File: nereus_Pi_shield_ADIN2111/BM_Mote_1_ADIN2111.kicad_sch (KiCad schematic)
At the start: 26 parts, among them U1 ADIN2111BCPZ, U2 AP22913CN4-7, U3 AP22913CN4-7, Y1 ABM11W-25.0000MHZ-6-K1Z-T3

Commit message: S4.d: footprints findable -- project library Vault (mote.pretty) extracted from the mote board; close S5.a
43 footprints the schematic uses, extracted read-only from the reference
board with KiCad 9.0.6 pcbnew (tools/fpextract.py, back-side parts
flipped, nets cleared), registered as nickname Vault to match the board
IDs; 118 bare footprint fields -> Vault:<name>. fpextract --verify: 0
problems (negative-tested). Netlist identical except footprint fields.
ERC 74/626 -> 74/508 (footprint-link warnings gone). D19.

Co-Authored-By: Claude Opus 5.5 <noreply@anthropic.com>
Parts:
- C1, C10, C11, C12, C13, C14, C3, C9: footprint FP-CL278-IPC_C -> Vault:FP-CL278-IPC_C
- C2, C4: footprint FP-CL511-IPC_C -> Vault:FP-CL511-IPC_C
- C5, C6: footprint FP-CC0402-MFG -> Vault:FP-CC0402-MFG
- C7, C8: footprint FP-CC0402-0_55-IPC_B -> Vault:FP-CC0402-0_55-IPC_B
- R1: footprint RESC1005X40X25ML05T10 -> Vault:RESC1005X40X25ML05T10
- R2, R3, R4, R5, R6: footprint RESC1005X40X25LL05T05 -> Vault:RESC1005X40X25LL05T05
- TP1, TP2: footprint PCB_TP_1.5mm -> Vault:PCB_TP_1.5mm
- U1: footprint ADIN2111BCPZ-Footprint-1 -> Vault:ADIN2111BCPZ-Footprint-1
- U2, U3: footprint AP22913CN4-7-Footprint-1 -> Vault:AP22913CN4-7-Footprint-1
- Y1: footprint FP-ABM11W-MFG -> Vault:FP-ABM11W-MFG
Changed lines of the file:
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@@
 			)
 		)
-		(property "Footprint" "PCB_TP_1.5mm"
+		(property "Footprint" "Vault:PCB_TP_1.5mm"
 			(at 185.42 200.4822 0)
 			(effects
@@
 			)
 		)
-		(property "Footprint" "RESC1005X40X25ML05T10"
+		(property "Footprint" "Vault:RESC1005X40X25ML05T10"
 			(at 121.92 70.9422 0)
 			(effects
@@
 			)
 		)
-		(property "Footprint" ""
+				(property "Footprint" ""
 			(at 91.44 96.3422 0)
 			(effects
@@
 			)
 		)
-		(property "Footprint" ""
+				(property "Footprint" ""
 			(at 215.9 238.5822 0)
 			(effects
@@
 			)
 		)
-		(property "Footprint" ""
+				(property "Footprint" ""
 			(at 226.06 238.5822 0)
 			(effects
@@
 			)
 		)
-		(property "Footprint" "ADIN2111BCPZ-Footprint-1"
+		(property "Footprint" "Vault:ADIN2111BCPZ-Footprint-1"
 			(at 259.08 203.0222 0)
 			(effects
@@
 			)
 		)
-		(property "Footprint" "FP-CL278-IPC_C"
+		(property "Footprint" "Vault:FP-CL278-IPC_C"
 			(at 226.06 228.4222 0)
 			(effects
@@
 			)
 		)
-		(property "Footprint" "PCB_TP_1.5mm"
+		(property "Footprint" "Vault:PCB_TP_1.5mm"
 			(at 185.42 230.9622 0)
 			(effects
@@
 			)
 		)
-		(property "Footprint" ""
+				(property "Footprint" ""
 			(at 160.02 91.2622 0)
 			(effects
@@
 			)
 		)
-		(property "Footprint" "AP22913CN4-7-Footprint-1"
+		(property "Footprint" "Vault:AP22913CN4-7-Footprint-1"
 			(at 177.8 228.4222 0)
 			(effects
@@
 			)
 		)
-		(property "Footprint" ""
+				(property "Footprint" ""
 			(at 264.16 78.5622 0)
 			(effects
@@
 			)
 		)
-		(property "Footprint" ""
+				(property "Footprint" ""
 			(at 287.02 103.9622 0)
 			(effects
@@
 			)
 		)
-		(property "Footprint" "FP-CL278-IPC_C"
+		(property "Footprint" "Vault:FP-CL278-IPC_C"
 			(at 276.86 70.9422 0)
 			(effects
@@
 			)
 		)
-		(property "Footprint" "FP-CC0402-MFG"
+		(property "Footprint" "Vault:FP-CC0402-MFG"
 			(at 91.44 88.7222 0)
 			(effects
@@
 			)
 		)
-		(property "Footprint" ""
+				(property "Footprint" ""
 			(at 264.16 106.5022 0)
 			(effects
@@
 			)
 		)
-		(property "Footprint" "RESC1005X40X25LL05T05"
+		(property "Footprint" "Vault:RESC1005X40X25LL05T05"
 			(at 254 106.5022 0)
 			(effects
@@
 			)
 		)
-		(property "Footprint" ""
+				(property "Footprint" ""
 			(at 124.46 63.3222 0)
 			(effects
@@
 			)
 		)
-		(property "Footprint" ""
+				(property "Footprint" ""
 			(at 78.74 93.8022 0)
 			(effects
@@
 			)
 		)
-		(property "Footprint" ""
+				(property "Footprint" ""
 			(at 264.16 119.2022 0)
 			(effects
@@
 			)
 		)
-		(property "Footprint" "RESC1005X40X25LL05T05"
+		(property "Footprint" "Vault:RESC1005X40X25LL05T05"
 			(at 261.62 91.2622 0)
 			(effects
@@
 			)
 		)
-		(property "Footprint" ""
+				(property "Footprint" ""
 			(at 276.86 76.0222 0)
 			(effects
@@
 			)
 		)
-		(property "Footprint" ""
+				(property "Footprint" ""
 			(at 254 142.0622 0)
 			(effects
@@
 			)
 		)
-		(property "Footprint" ""
+				(property "Footprint" ""
 			(at 226.06 210.6422 0)
 			(effects
@@
 			)
 		)
-		(property "Footprint" "FP-CL278-IPC_C"
+		(property "Footprint" "Vault:FP-CL278-IPC_C"
 			(at 226.06 200.4822 0)
 			(effects
@@
 			)
 		)
-		(property "Footprint" ""
+				(property "Footprint" ""
 			(at 149.86 197.9422 0)
 			(effects
@@
 			)
 		)
-		(property "Footprint" "AP22913CN4-7-Footprint-1"
+		(property "Footprint" "Vault:AP22913CN4-7-Footprint-1"
 			(at 177.8 197.9422 0)
 			(effects
@@
 			)
 		)
-		(property "Footprint" "FP-CC0402-0_55-IPC_B"
+		(property "Footprint" "Vault:FP-CC0402-0_55-IPC_B"
 			(at 254 131.9022 0)
 			(effects
@@
 			)
 		)
-		(property "Footprint" "ADIN2111BCPZ-Footprint-1"
+		(property "Footprint" "Vault:ADIN2111BCPZ-Footprint-1"
 			(at 205.74 98.8822 0)
 			(effects
@@
 			)
 		)
-		(property "Footprint" "FP-CC0402-0_55-IPC_B"
+		(property "Footprint" "Vault:FP-CC0402-0_55-IPC_B"
 			(at 287.02 131.9022 0)
 			(effects
@@
 			)
 		)
-		(property "Footprint" "FP-ABM11W-MFG"
+		(property "Footprint" "Vault:FP-ABM11W-MFG"
 			(at 259.08 131.9022 0)
 			(effects
@@
 			)
 		)
-		(property "Footprint" ""
+				(property "Footprint" ""
 			(at 149.86 228.4222 0)
 			(effects
@@
 			)
 		)
-		(property "Footprint" "RESC1005X40X25LL05T05"
+		(property "Footprint" "Vault:RESC1005X40X25LL05T05"
 			(at 266.7 103.9622 0)
 			(effects
@@
 			)
 		)
-		(property "Footprint" "FP-CL511-IPC_C"
+		(property "Footprint" "Vault:FP-CL511-IPC_C"
 			(at 292.1 68.4022 0)
 			(effects
@@
 			)
 		)
-		(property "Footprint" ""
+				(property "Footprint" ""
 			(at 193.04 210.6422 0)
 			(effects
@@
 			)
 		)
-		(property "Footprint" "FP-CL278-IPC_C"
+		(property "Footprint" "Vault:FP-CL278-IPC_C"
 			(at 304.8 65.8622 0)
 			(effects
@@
 			)
 		)
-		(property "Footprint" "RESC1005X40X25LL05T05"
+		(property "Footprint" "Vault:RESC1005X40X25LL05T05"
 			(at 254 98.8822 0)
 			(effects
@@
 			)
 		)
-		(property "Footprint" ""
+				(property "Footprint" ""
 			(at 292.1 73.4822 0)
 			(effects
@@
 			)
 		)
-		(property "Footprint" ""
+				(property "Footprint" ""
 			(at 215.9 210.6422 0)
 			(effects
@@
 			)
 		)
-		(property "Footprint" ""
+				(property "Footprint" ""
 			(at 304.8 70.9422 0)
 			(effects
@@
 			)
 		)
-		(property "Footprint" "FP-CL511-IPC_C"
+		(property "Footprint" "Vault:FP-CL511-IPC_C"
 			(at 264.16 73.4822 0)
 			(effects
@@
 			)
 		)
-		(property "Footprint" "FP-CL278-IPC_C"
+		(property "Footprint" "Vault:FP-CL278-IPC_C"
 			(at 215.9 228.4222 0)
 			(effects
@@
 			)
 		)
-		(property "Footprint" ""
+				(property "Footprint" ""
 			(at 205.74 210.6422 0)
 			(effects
@@
 			)
 		)
-		(property "Footprint" "FP-CL278-IPC_C"
+		(property "Footprint" "Vault:FP-CL278-IPC_C"
 			(at 215.9 200.4822 0)
 			(effects
@@
 			)
 		)
-		(property "Footprint" "RESC1005X40X25LL05T05"
+		(property "Footprint" "Vault:RESC1005X40X25LL05T05"
 			(at 254 119.2022 0)
 			(effects
@@
 			)
 		)
-		(property "Footprint" "FP-CC0402-MFG"
+		(property "Footprint" "Vault:FP-CC0402-MFG"
 			(at 78.74 86.1822 0)
 			(effects
@@
 			)
 		)
-		(property "Footprint" ""
+				(property "Footprint" ""
 			(at 287.02 91.2622 0)
 			(effects
@@
 			)
 		)
-		(property "Footprint" "FP-CL278-IPC_C"
+		(property "Footprint" "Vault:FP-CL278-IPC_C"
 			(at 193.04 200.4822 0)
 			(effects
@@
 			)
 		)
-		(property "Footprint" "FP-CL278-IPC_C"
+		(property "Footprint" "Vault:FP-CL278-IPC_C"
 			(at 205.74 200.4822 0)
 			(effects
@@
 			)
 		)
-		(property "Footprint" ""
+				(property "Footprint" ""
 			(at 264.16 98.8822 0)
 			(effects
@@
 			)
 		)
-		(property "Footprint" ""
+				(property "Footprint" ""
 			(at 287.02 142.0622 0)
 			(effects

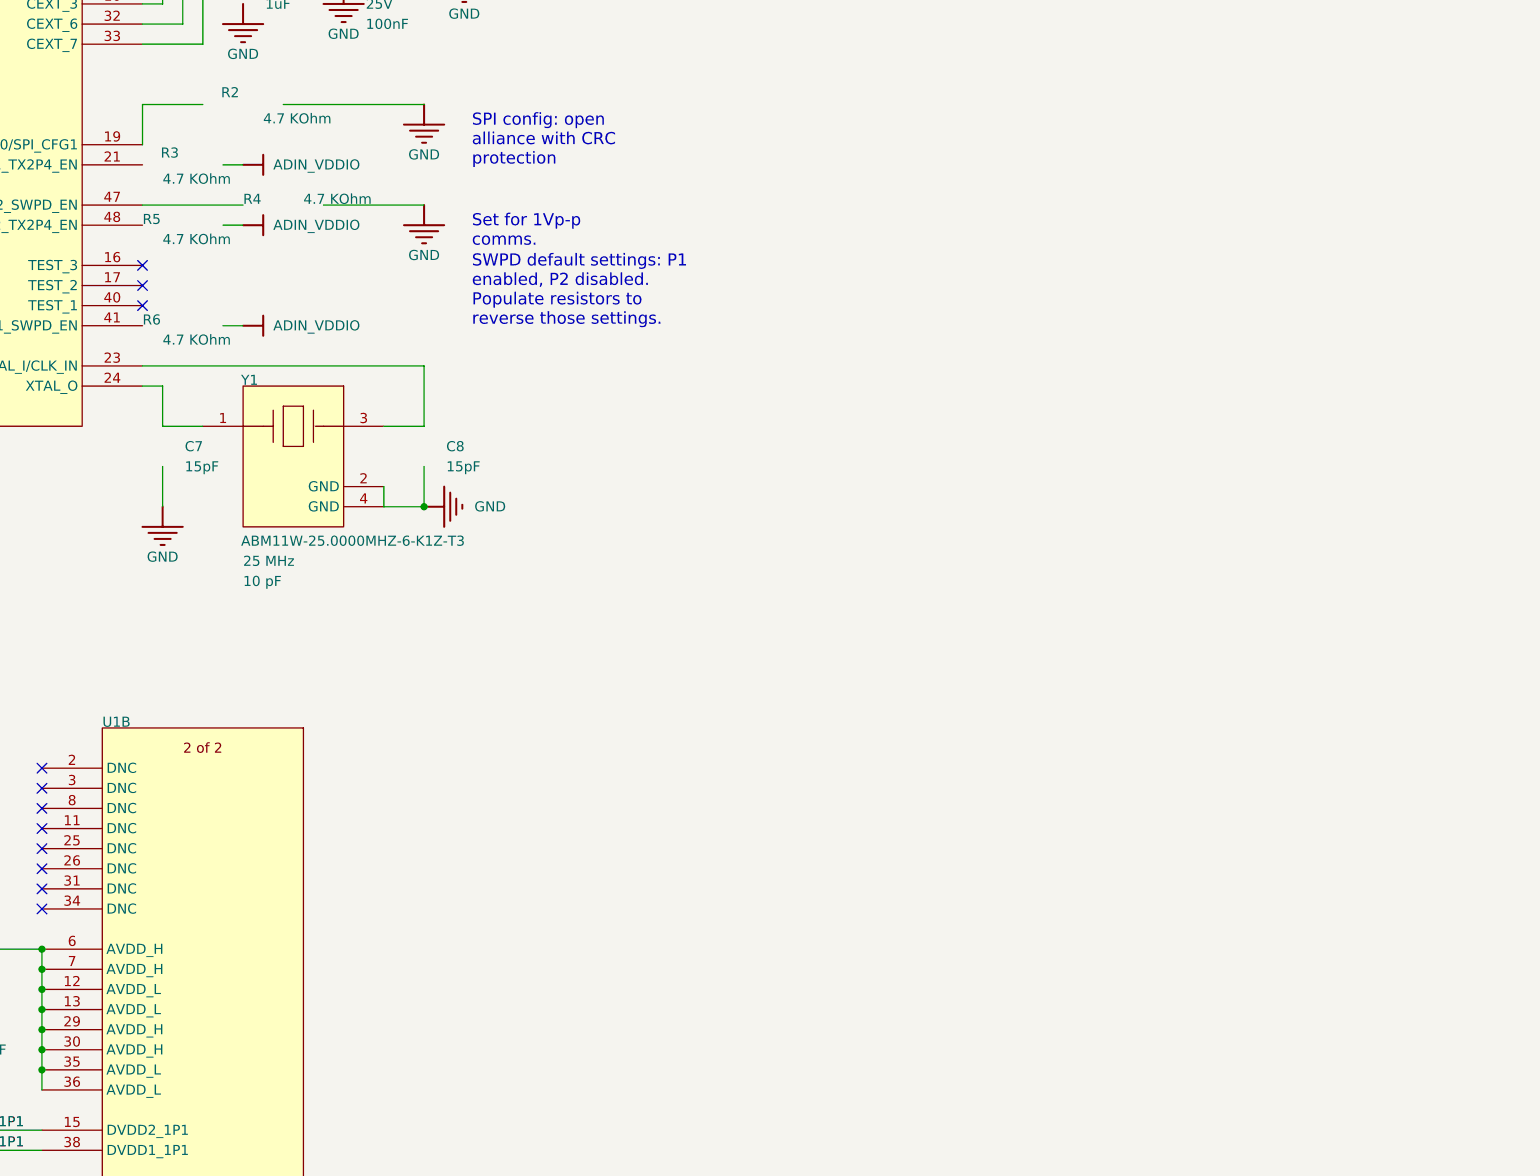
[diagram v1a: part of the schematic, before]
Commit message: S5.f: ADIN status LEDs -- D8 red (ADIN powered), D9 yellow-green (pin 21 link/activity), JP2 cut-to-disable
KT-0603R (C2286) / KT-0603YG (C2289), R44/R45 1.5k (R1's part), JP2 = JP1's
bridged net-tie footprint from ADIN_VDDIO. D9 active low on P1_LED_1 with R3 as
pull-up (strap unchanged). R3 redrawn in the LED group (connections unchanged),
U1 pin 21 stub + label ADIN_P1_LED1. ERC 27/506; netcheck 51/51. D25.

Co-Authored-By: Claude Opus 5.5 <noreply@anthropic.com>
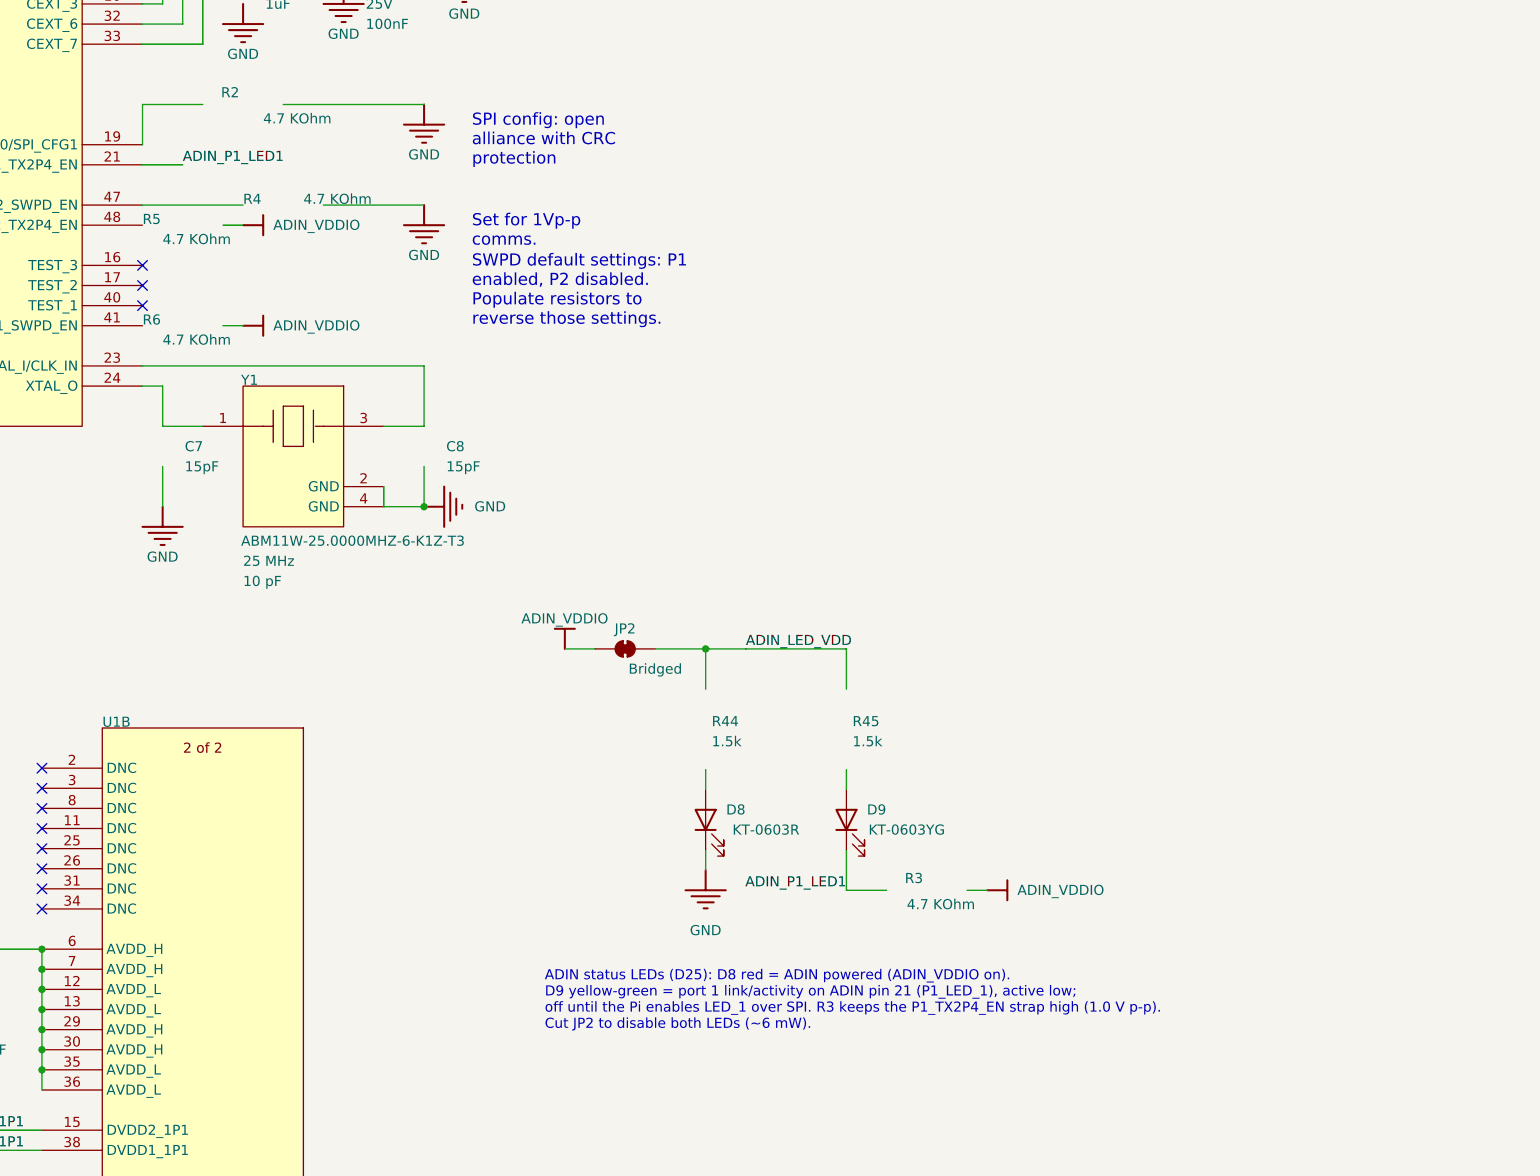
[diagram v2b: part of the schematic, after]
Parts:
- added D8: KT-0603R, LED_SMD:LED_0603_1608Metric, symbol Device:LED
- added D9: KT-0603YG, LED_SMD:LED_0603_1608Metric, symbol Device:LED
- added JP2: Bridged, nereus:SolderJumper-2_R1210_Bridged_NetTie, symbol Jumper:SolderJumper_2_Bridged
- added R44, R45: RC0402FR-071K5L, Vault:RESC1005X40X25ML05T10, symbol BM_Mote_000639-AB-altium-import:ADIN_1_RES_Altium Content Vault_0
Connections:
- net ADIN_VDDIO: now also JP2.1 (A)
- net GND: now also D8.1 (K)
- net ADIN_P1_LED1: now reaches U1.21 (P1_LED_1/P1_TX2P4_EN)
- net ADIN_P1_LED1: now also D9.1 (K)
- new net ADIN_LED_VDD: JP2.2 (B)
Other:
- note added: "ADIN status LEDs (D25): D8 red = ADIN powered (ADIN_VDDIO on). D9 yellow-green = port 1 link/activity on ADIN pin 21 (P1_LED_1), active low; off until the Pi enables LED_1 over SPI. R3 keeps the P1_TX2P4_EN strap high (1.0 V p-p). Cut JP2 to disable both LEDs (~6 mW)."
